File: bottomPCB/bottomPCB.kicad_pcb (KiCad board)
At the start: 2 copper layers, 184.8 x 139 mm, 46 parts, among them J1 Conn_01x03_Pin, J2 Conn_02x03_Odd_Even, J3 Conn_01x02, J4 Conn_02x03_Odd_Even, J5 1-84953-1, J6 1-84953-1, J7 1-84953-1, J8 1-84953-1, U1 ESP32-WROOM-32, U2 XT30_horizontal, U8 LM1117IMPX-3_3_NOPB, U9 LM1117IMPX-3_3_NOPB

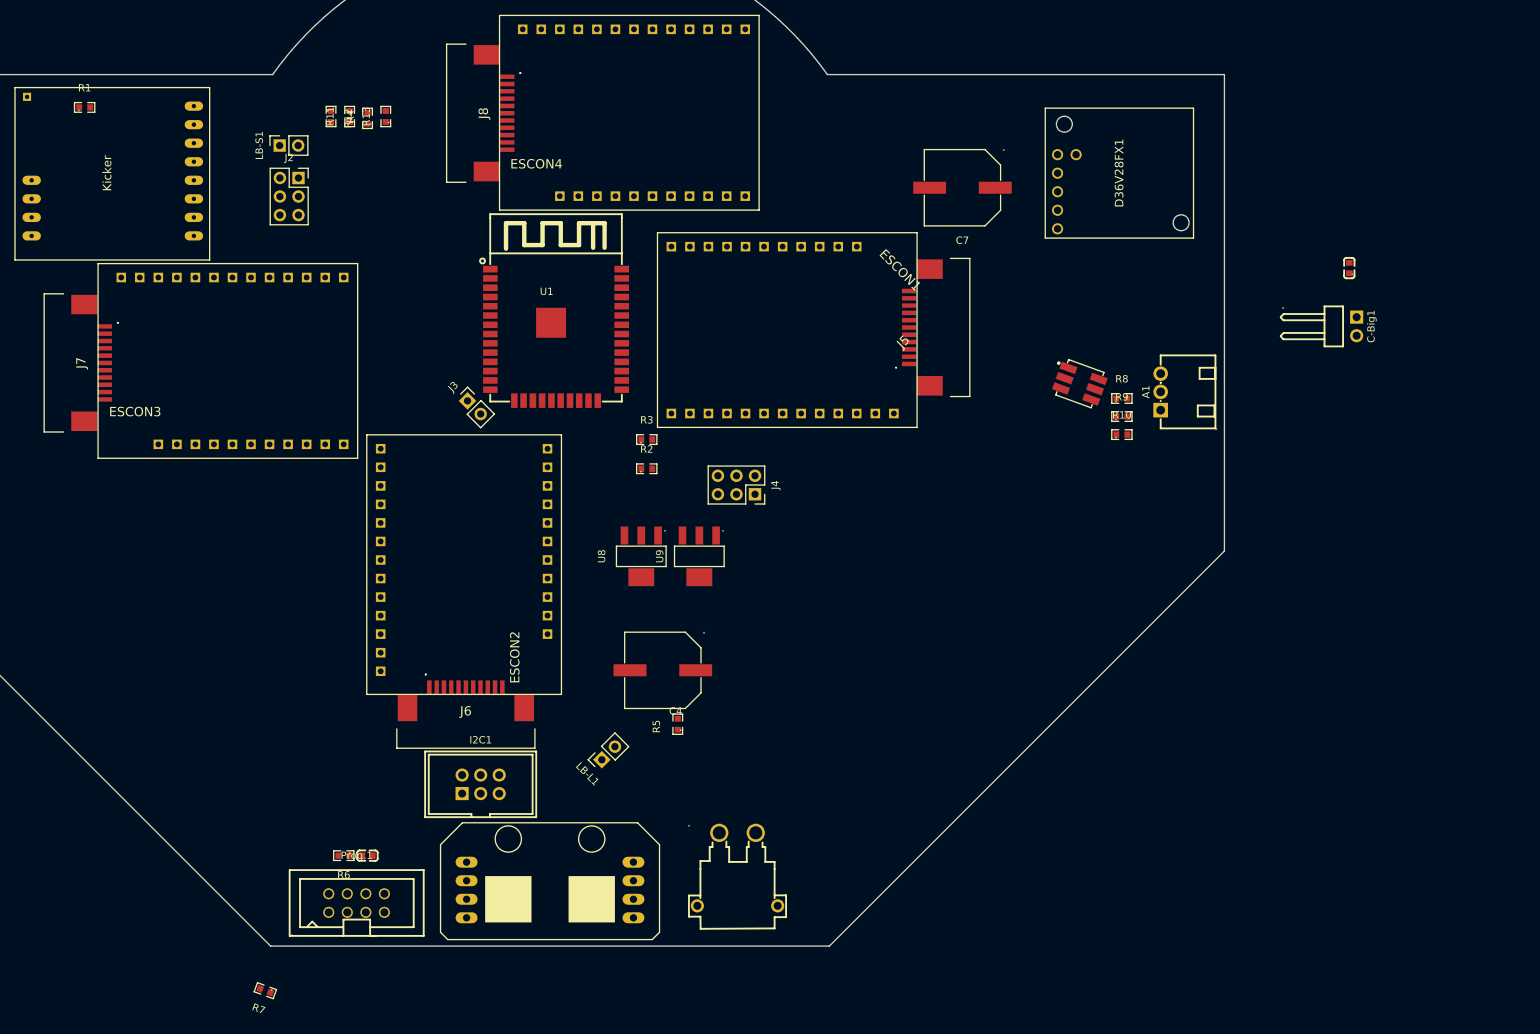
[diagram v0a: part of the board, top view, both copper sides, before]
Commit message: replaced smd connectors for ec flat with BohleBots standard
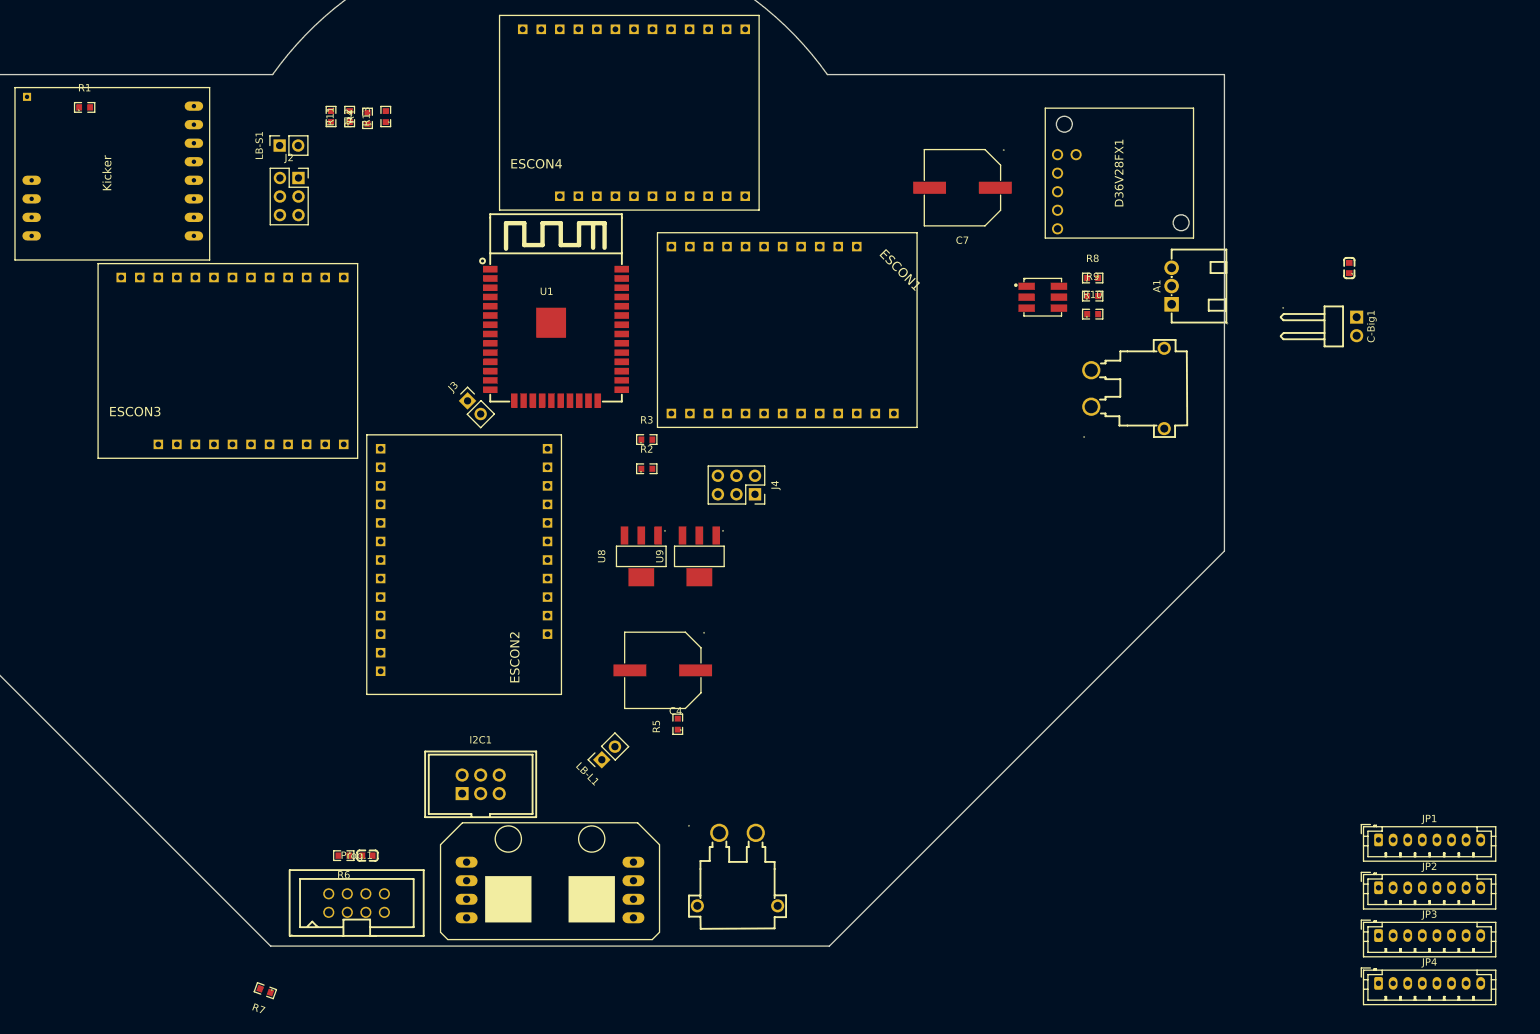
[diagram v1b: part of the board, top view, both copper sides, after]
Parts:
- removed J5, J6, J7, J8: 1-84953-1, 1-84953-1:1849531
- added JP1: B8B-PH-K, Connector_JST:JST_PH_B8B-PH-K_1x08_P2.00mm_Vertical, F.Cu at (123.5, 87.8)
- added JP2: B8B-PH-K, Connector_JST:JST_PH_B8B-PH-K_1x08_P2.00mm_Vertical, F.Cu at (123.5, 94.4)
- added JP3: B8B-PH-K, Connector_JST:JST_PH_B8B-PH-K_1x08_P2.00mm_Vertical, F.Cu at (123.5, 101.0)
- added JP4: B8B-PH-K, Connector_JST:JST_PH_B8B-PH-K_1x08_P2.00mm_Vertical, F.Cu at (123.5, 107.5)
- added U3: XT30_horizontal, BohleBots:CONN-TH_XT30PW-M, F.Cu at (89.1, 26.0)
- moved R10 17.0 mm to (84.3, 15.8)
- moved R8 17.0 mm to (84.3, 10.9)
- moved R9 17.0 mm to (84.3, 13.3)
- moved A1 14.6 mm to (95.2, 12.0)
- moved LED1 12.9 mm to (77.5, 13.5), turned to 0 degrees
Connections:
- A1 pad 1: +BATT -> Net-(A1-Pad1)

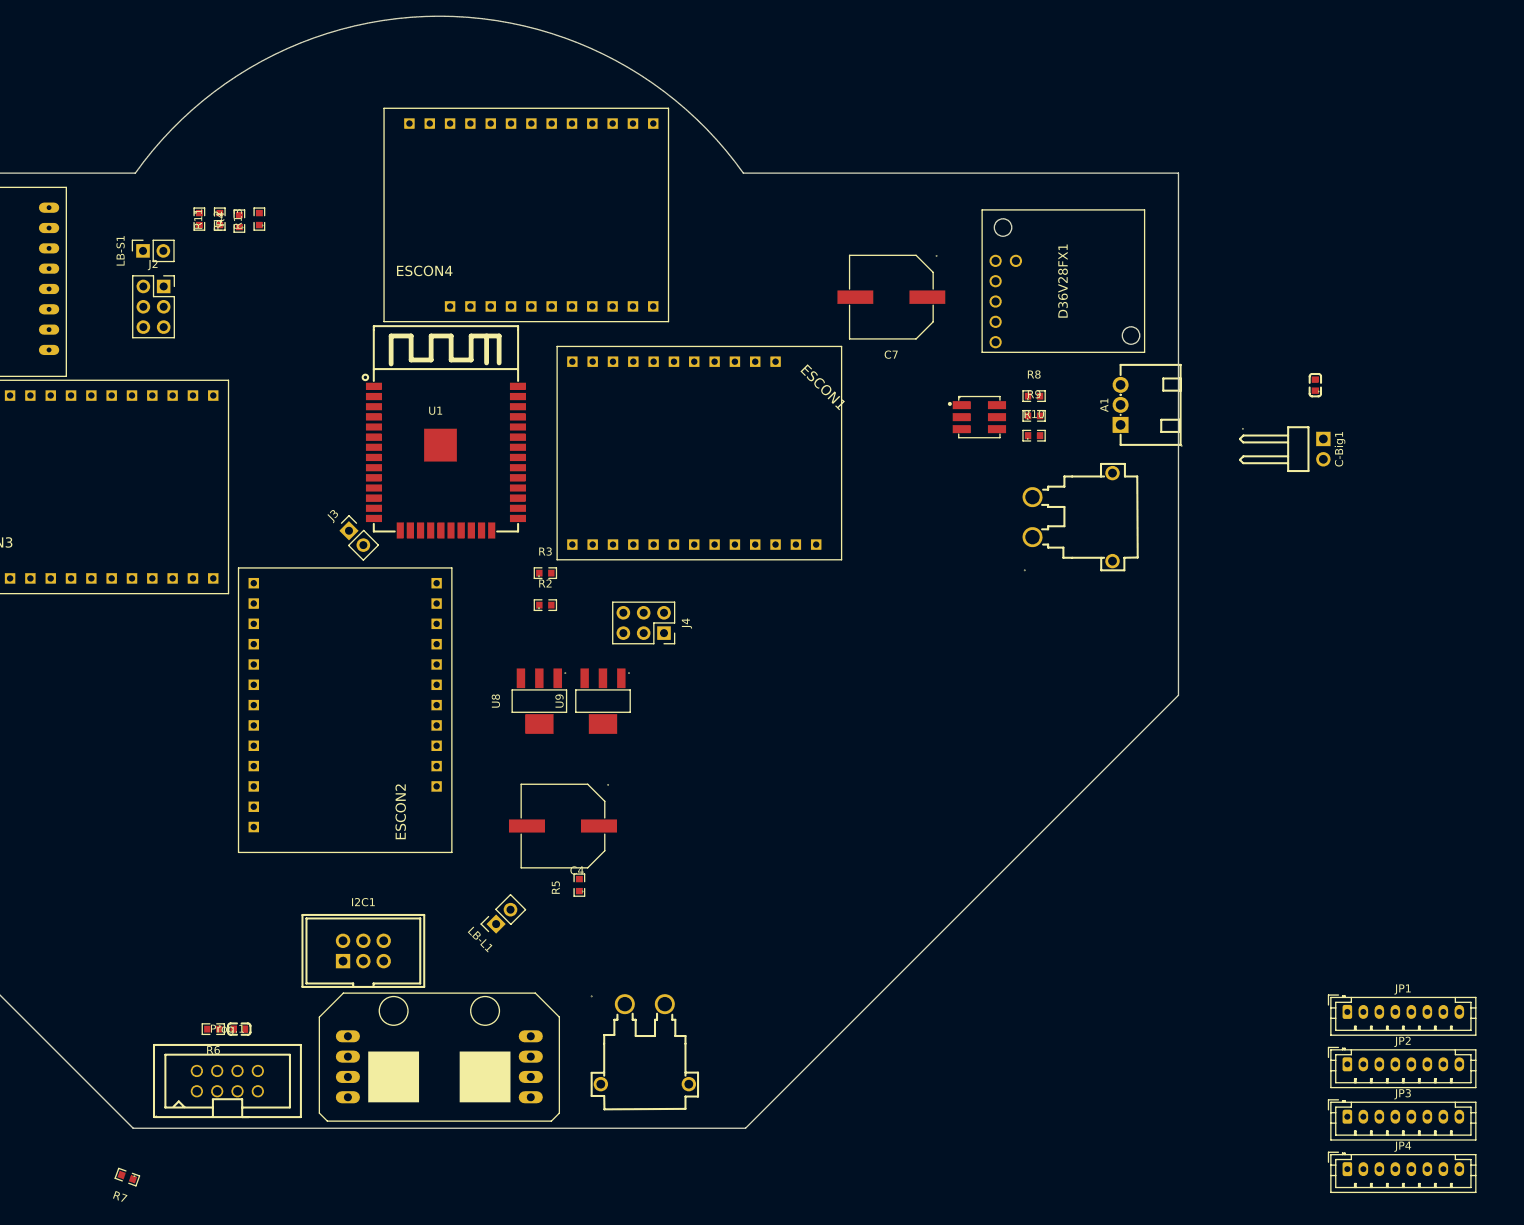
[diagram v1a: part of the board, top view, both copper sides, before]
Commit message: set standard connectors for motors
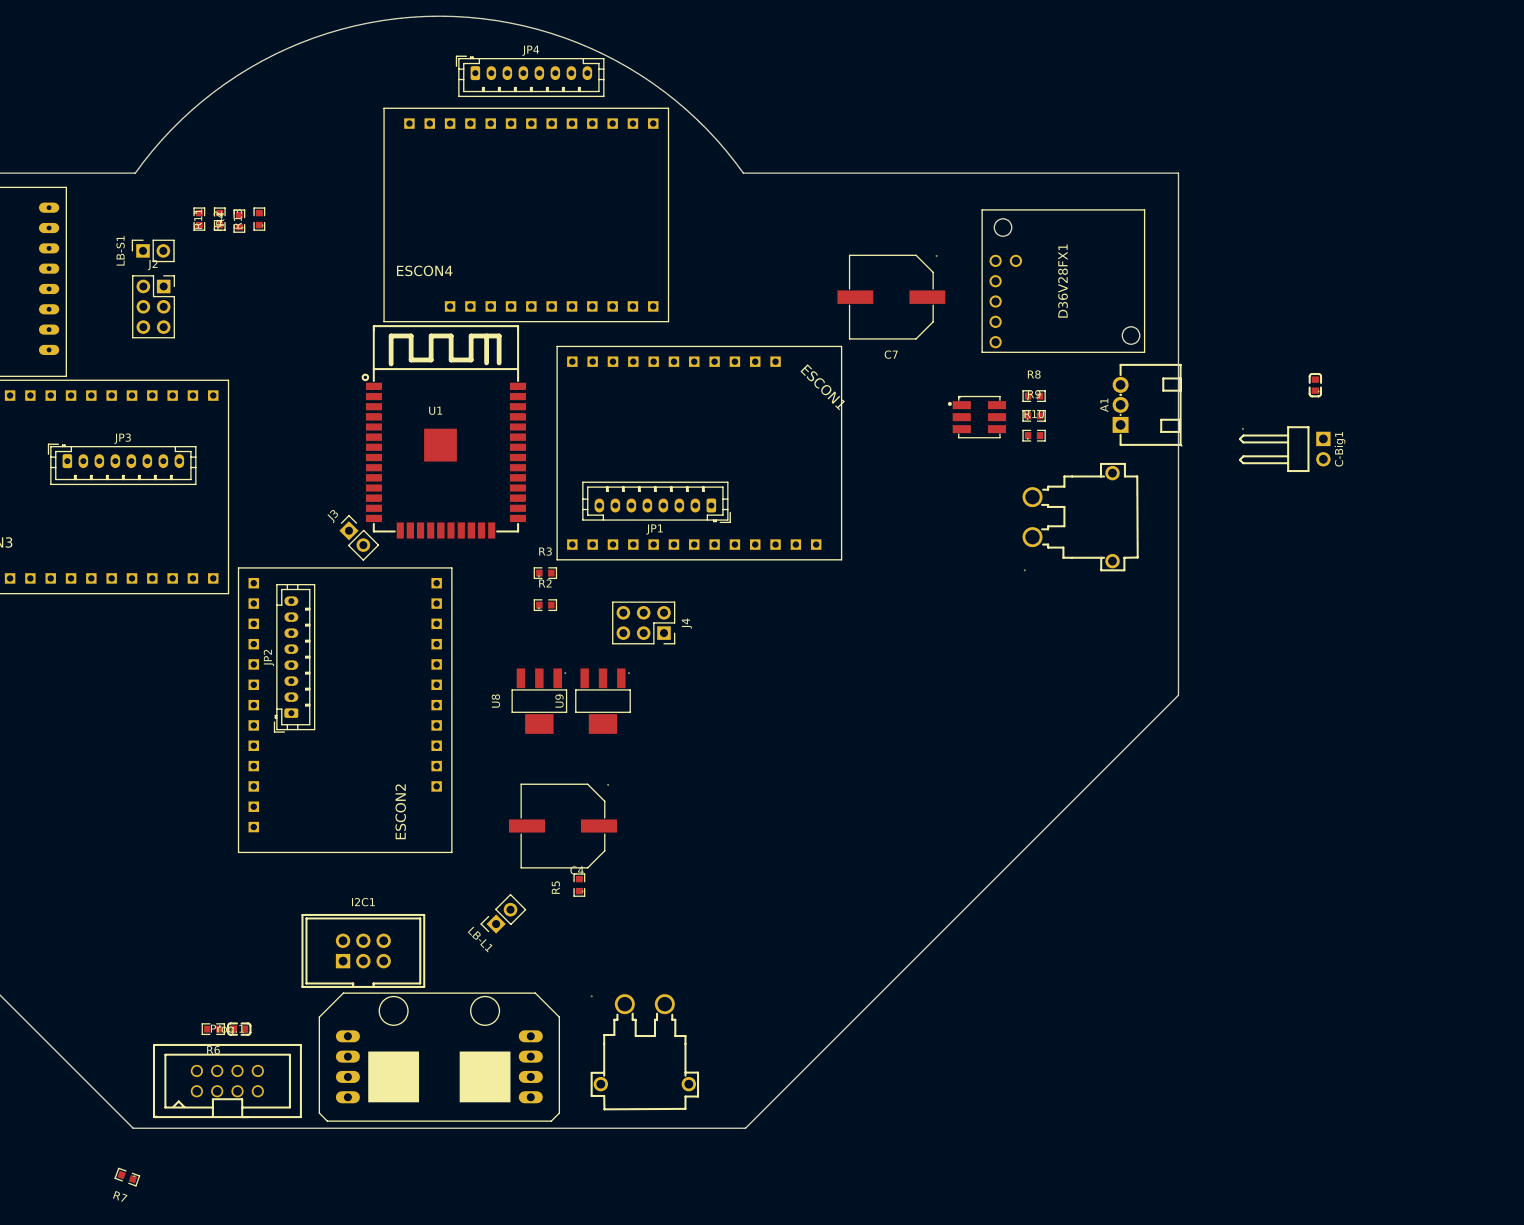
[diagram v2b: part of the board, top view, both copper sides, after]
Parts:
- moved JP3 179.8 mm to (-36.5, 19.0)
- moved JP4 175.1 mm to (14.5, -29.5)
- moved JP2 139.1 mm to (-8.50, 50.5), turned to 90 degrees
- moved JP1 101.6 mm to (44.0, 24.6), turned to 180 degrees
